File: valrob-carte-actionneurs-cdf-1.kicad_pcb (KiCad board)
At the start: 4 copper layers, 50 x 50 mm, 126 parts, among them J1 USB_C_Receptacle_USB2.0_14P, J2 Conn_01x02, J3 Conn_01x02, J4 Conn_01x04_Pin, J5 Conn_01x02, J6 Conn_01x02, J7 Conn_01x12, M1 Motor_Servo, M10 Motor_Servo, M11 Motor_Servo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

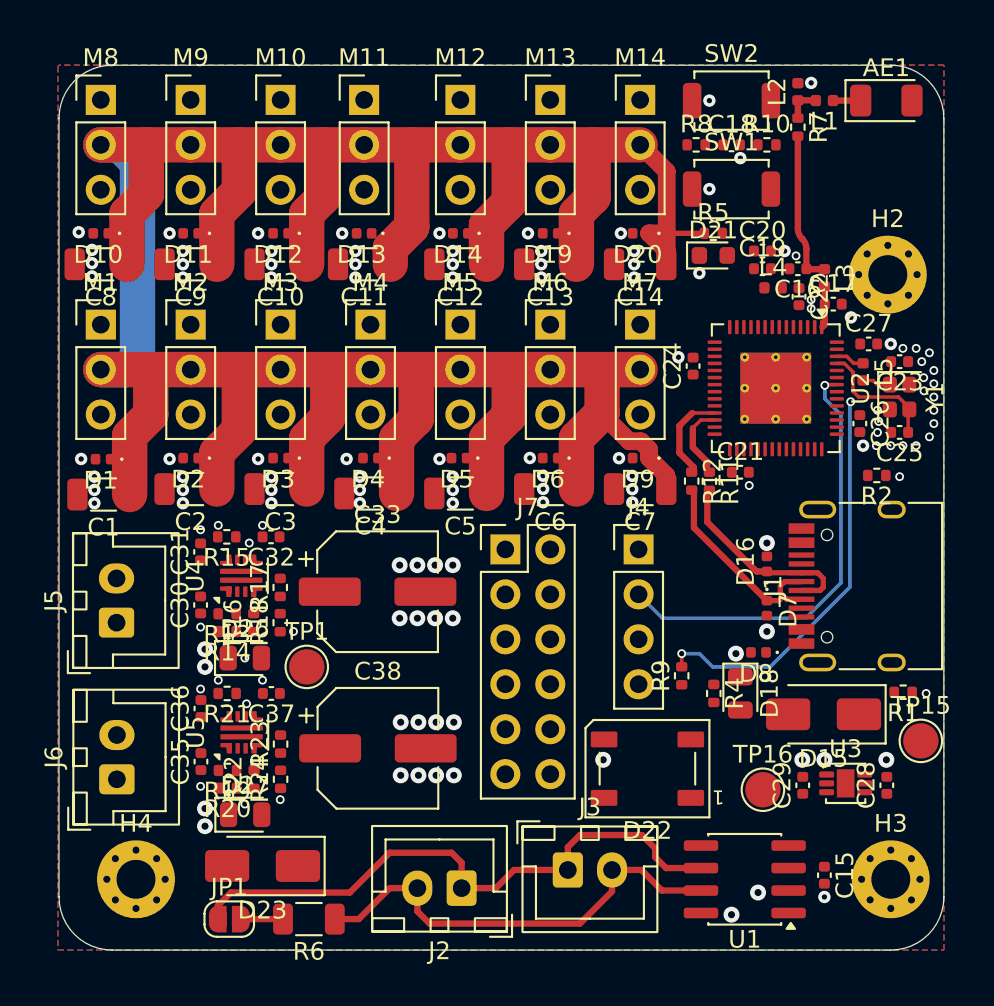
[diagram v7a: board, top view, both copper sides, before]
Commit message: pcb: add efuse and 5v pwr routing
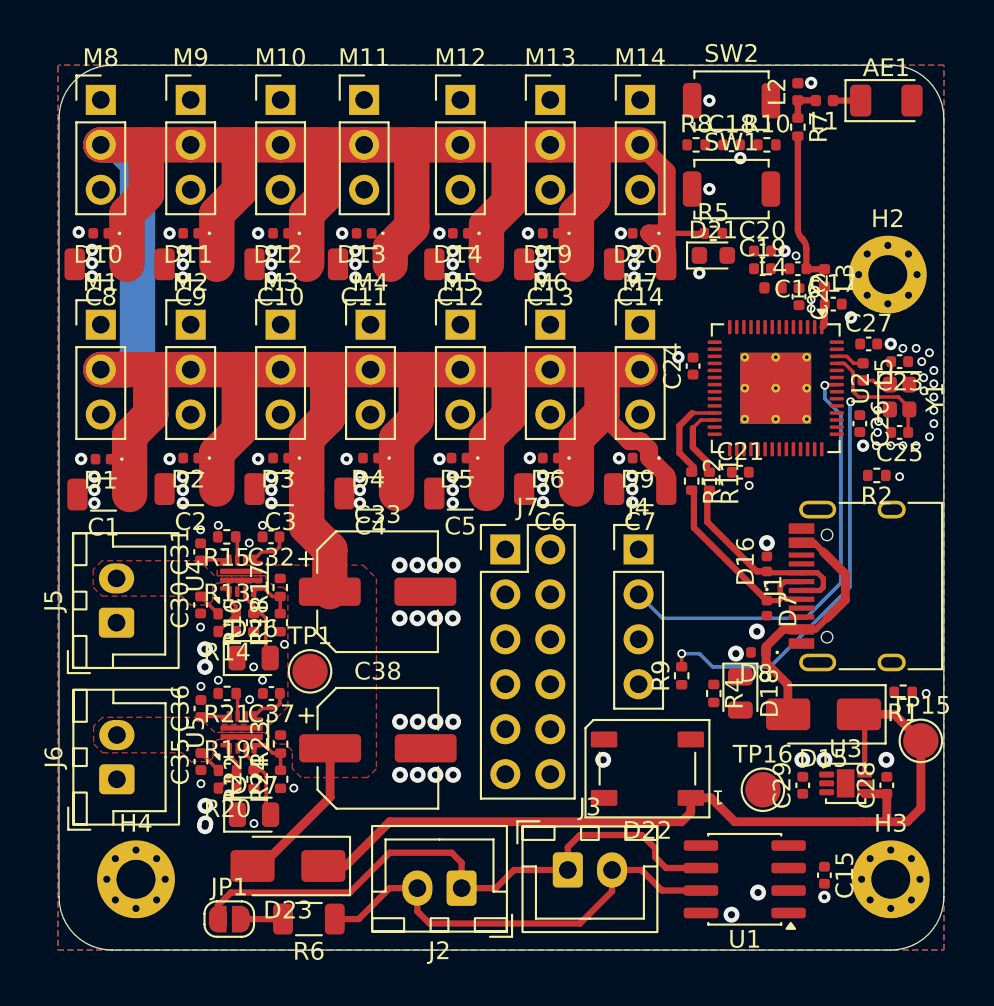
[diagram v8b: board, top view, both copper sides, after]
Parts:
- moved D23 1.44 mm to (96.9, 104.2)
- moved D26 0.50 mm to (95.0, 92.5)
- moved D27 0.50 mm to (95.0, 101.3)
- moved TP1 0.31 mm to (98.2, 93.2)
- turned R13 to 0 degrees
- turned R19 to 0 degrees
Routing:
- net +5V_MCU: track 0.00 -> 51.1 mm
- net +5V: track 182.7 -> 197.8 mm
- net +Vbus: track 0.00 -> 14.9 mm
- net /PG_B: track 0.00 -> 4.58 mm
- net /PG_A: track 0.00 -> 4.58 mm
- net Net-(U4-EN/UVLO): track 0.00 -> 2.85 mm
- net Net-(U5-EN/UVLO): track 0.00 -> 2.85 mm
- net Net-(U4-PGTH): track 0.00 -> 2.74 mm
- net Net-(U5-PGTH): track 0.00 -> 2.74 mm
- net Net-(U5-DVDT): track 0.00 -> 2.34 mm
- net Net-(U4-DVDT): track 0.00 -> 2.34 mm
- net Net-(U5-ITIMER): track 0.00 -> 1.61 mm
- net Net-(U4-ITIMER): track 0.00 -> 1.61 mm
- net Net-(J6-Pin_2): track 0.00 -> 1.40 mm
- net Net-(J5-Pin_2): track 0.00 -> 1.40 mm
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- added copper zone on F.Cu, net +5V
- added copper zone on F.Cu, net Net-(J5-Pin_2)
- added copper zone on F.Cu, net Net-(J6-Pin_2)
